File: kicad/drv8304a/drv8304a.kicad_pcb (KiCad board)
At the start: 2 copper layers, 37 parts, among them J1 Conn_01x05_Pin, J2 Conn_01x03_Pin, J3 Conn_01x05_Pin, Q1 CSD18514Q5A, Q2 CSD18514Q5A, Q3 CSD18514Q5A, Q4 CSD18514Q5A, Q5 CSD18514Q5A, Q6 CSD18514Q5A, U1 DRV8304H

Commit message: some routing
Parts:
- added C11: 1uF, Capacitor_SMD:C_0805_2012Metric_Pad1.18x1.45mm_HandSolder, F.Cu at (184.0, 84.5)
- added C12: 1uF, Capacitor_SMD:C_0805_2012Metric_Pad1.18x1.45mm_HandSolder, F.Cu at (184.0, 96.5)
- added C13: 1uF, Capacitor_SMD:C_0805_2012Metric_Pad1.18x1.45mm_HandSolder, F.Cu at (178.0, 108.5)
- added J4: Conn_01x02_Pin, Connector_PinHeader_2.54mm:PinHeader_1x02_P2.54mm_Vertical, F.Cu at (30.8, 26.8)
- moved Q1 159.9 mm to (190.0, 110.0), turned to 180 degrees
- moved Q2 155.0 mm to (190.0, 104.0)
- moved J2 151.9 mm to (200.0, 100.0), turned to 90 degrees
- moved Q3 150.9 mm to (190.0, 98.0), turned to 180 degrees
- moved Q4 147.9 mm to (190.0, 92.0)
- moved Q5 145.9 mm to (190.0, 86.0), turned to 180 degrees
- moved Q6 145.0 mm to (190.0, 80.0)
- moved R14 133.6 mm to (184.1, 105.5), turned to -90 degrees
- moved R15 125.3 mm to (173.0, 112.8)
- moved R16 125.3 mm to (173.0, 117.7)
- moved U1 118.8 mm to (170.0, 95.0), turned to 90 degrees
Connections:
- net Net-(J2-Pin_1) renamed /SHA
- net Net-(J2-Pin_2) renamed /SHB
- net Net-(J2-Pin_3) renamed /SHC
- net Net-(Q1-D) renamed VM
- net Net-(Q1-G) renamed /GHA
- net Net-(Q2-G) renamed /GLA
- net Net-(Q3-G) renamed /GHB
- net Net-(Q4-G) renamed /GLB
- net Net-(Q5-G) renamed /GHC
- net Net-(Q6-G) renamed /GLC
- net Net-(U1-SPA) renamed /SPA
- net Net-(U1-SPB) renamed /SPB
- net Net-(U1-SPC) renamed /SPC
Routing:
- net /GHA: track 0.00 -> 28.6 mm
- net /SHA: track 0.00 -> 26.6 mm
- net VM: track 0.00 -> 26.0 mm
- net /GLA: track 0.00 -> 21.0 mm

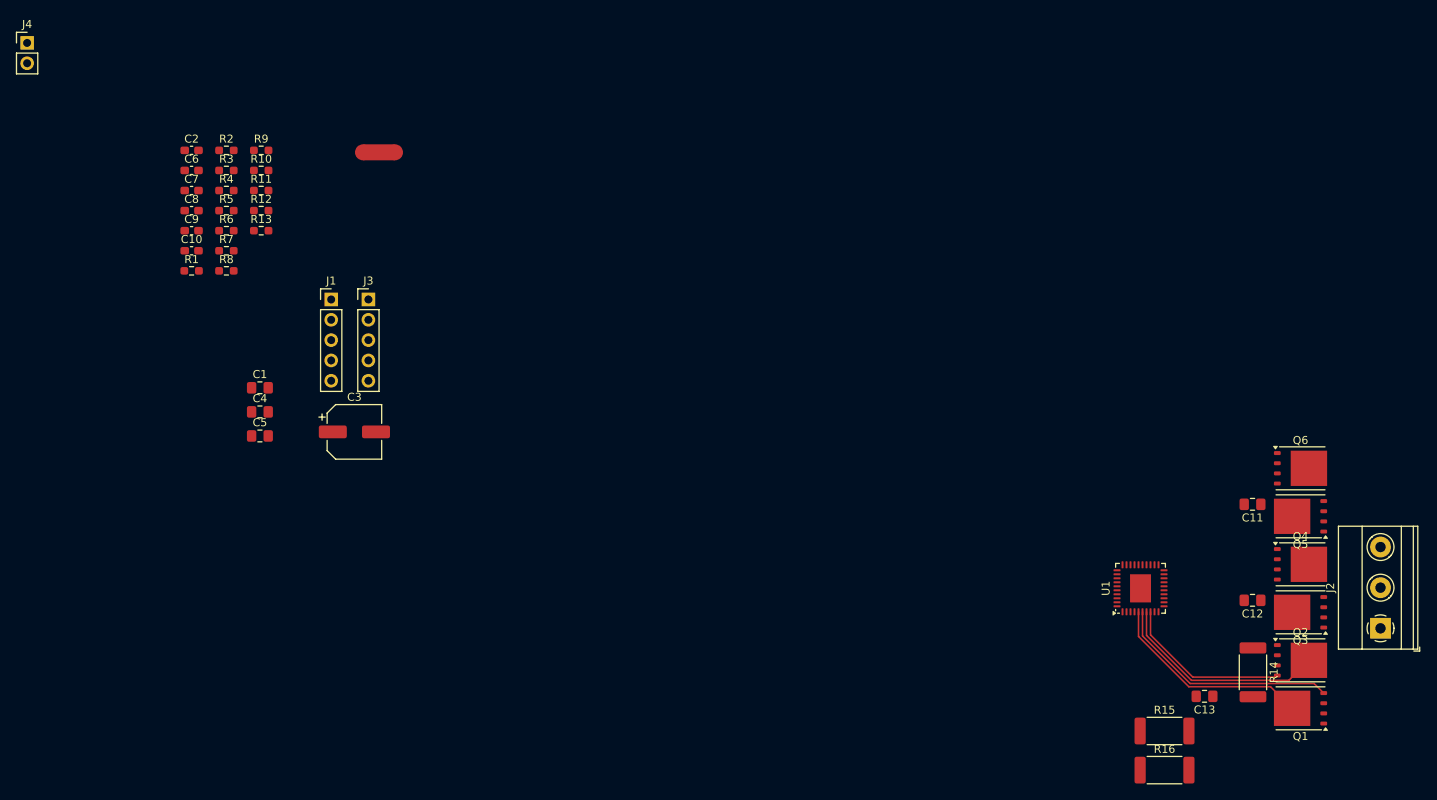
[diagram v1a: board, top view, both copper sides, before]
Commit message: FETS routed
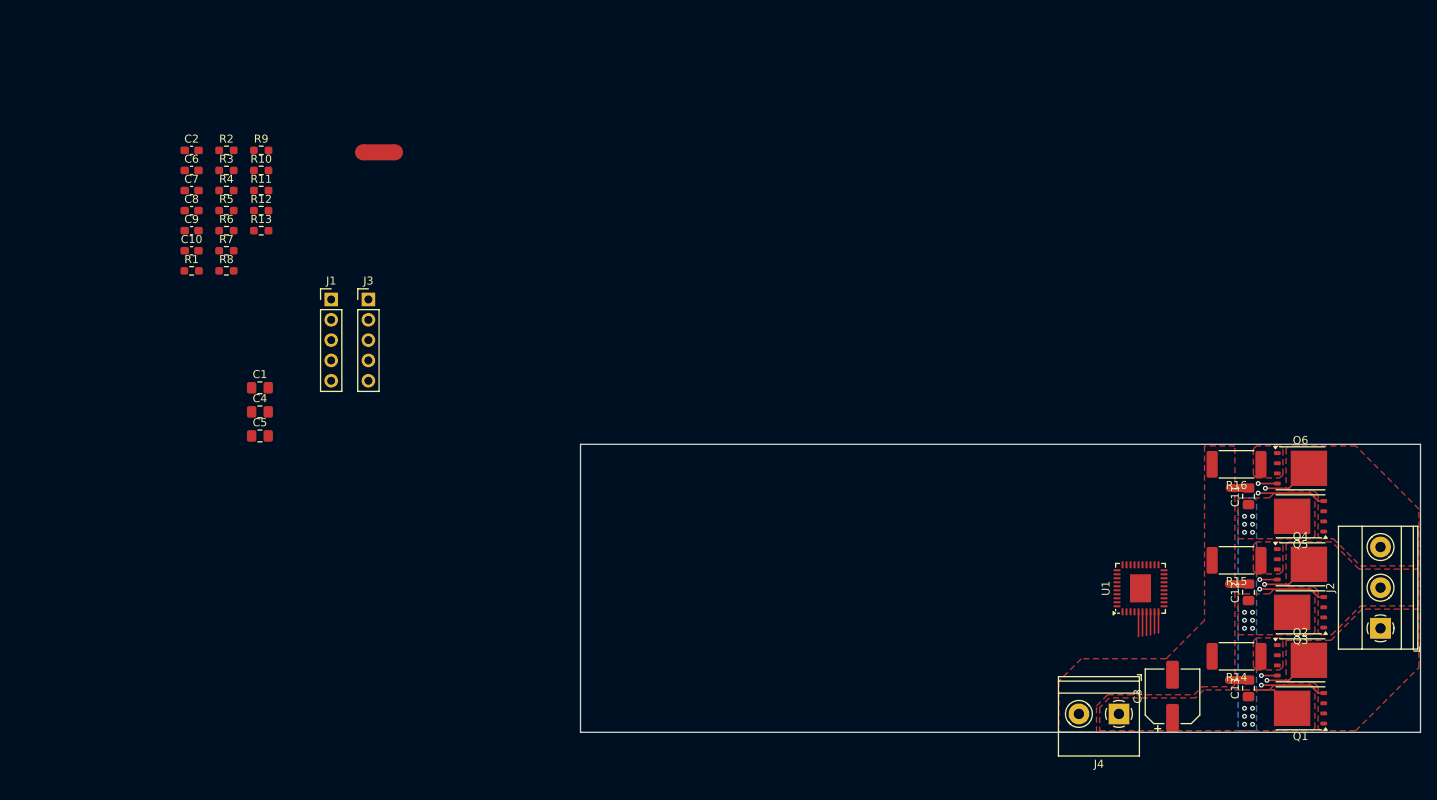
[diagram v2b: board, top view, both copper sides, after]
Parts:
- J4: footprint Connector_PinHeader_2.54mm:PinHeader_1x02_P2.54mm_Vertical -> TerminalBlock_Phoenix:TerminalBlock_Phoenix_MKDS-1,5-2_1x02_P5.00mm_Horizontal
- moved J4 160.2 mm to (167.3, 110.7), turned to 180 degrees
- moved C3 107.5 mm to (174.0, 108.5), turned to 90 degrees
- moved R16 39.3 mm to (182.0, 79.5), turned to 180 degrees
- moved R15 23.2 mm to (182.0, 91.5), turned to 180 degrees
- moved C13 5.59 mm to (183.5, 107.5), turned to 90 degrees
- moved R14 2.87 mm to (182.0, 103.5), turned to 180 degrees
- moved C11 1.12 mm to (183.5, 83.5), turned to 90 degrees
- moved C12 1.12 mm to (183.5, 95.5), turned to 90 degrees
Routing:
- net /GHA: track 28.6 -> 11.2 mm, vias 0 -> 1
- net /SHA: track 26.6 -> 9.24 mm, vias 0 -> 1
- net VM: track 26.0 -> 8.77 mm, vias 0 -> 18
- net /GLA: track 21.0 -> 4.88 mm, vias 0 -> 1
- net GNDPWR: track 0.00 -> 9.93 mm
- net /GHC: track 0.00 -> 8.68 mm, vias 0 -> 1
- net /GHB: track 0.00 -> 8.42 mm, vias 0 -> 1
- net /SHB: track 0.00 -> 6.59 mm, vias 0 -> 1
- net /SHC: track 0.00 -> 6.49 mm, vias 0 -> 1
- net /SPA: track 0.00 -> 3.66 mm
- net /GLC: track 0.00 -> 2.41 mm, vias 0 -> 1
- net /GLB: track 0.00 -> 2.20 mm, vias 0 -> 1
- added copper zone on F.Cu, net /SHA
- added copper zone on F.Cu, net /SHB
- added copper zone on F.Cu, net /SHC
- added copper zone on F.Cu, net /SPA
- added copper zone on F.Cu, net /SPB
- added copper zone on F.Cu, net /SPC
- added copper zone on F.Cu, net GNDPWR
- added copper zone on B.Cu, net VM
- added copper zone on F.Cu, net VM
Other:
- board outline added: 105 x 36 mm
- copper layers 2 -> 4

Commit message: lots routed
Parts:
- moved C2 132.9 mm to (169.6, 100.9)
- moved C6 122.6 mm to (161.7, 96.3), turned to 90 degrees
- moved C7 122.0 mm to (164.6, 90.8), turned to 180 degrees
- moved R2 121.4 mm to (169.9, 81.6), turned to 180 degrees
- moved R3 121.1 mm to (169.9, 83.1), turned to 180 degrees
- moved R1 121.1 mm to (169.9, 80.1), turned to 180 degrees
- moved R4 120.7 mm to (169.9, 84.6), turned to 180 degrees
- moved R5 120.4 mm to (169.9, 86.1), turned to 180 degrees
- moved C8 117.7 mm to (160.3, 92.5)
- moved C1 116.7 mm to (172.3, 101.5), turned to 90 degrees
- moved C9 115.8 mm to (160.3, 89.5)
- moved R9 114.9 mm to (166.1, 84.6), turned to 180 degrees
- moved R10 114.5 mm to (166.1, 86.1), turned to 180 degrees
- moved R6 114.3 mm to (166.1, 80.1), turned to 180 degrees
- moved R7 114.1 mm to (166.1, 81.6), turned to 180 degrees
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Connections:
- C7 pad 1: Net-(U1-VREF) -> VDD
- U1 pad 24: Net-(U1-VREF) -> VDD
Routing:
- net GNDPWR: track 9.93 -> 49.3 mm, vias 0 -> 3
- net VDD: track 0.00 -> 36.0 mm, vias 0 -> 3
- net GNDA: track 0.00 -> 24.9 mm, vias 0 -> 5
- net /SPC: track 0.00 -> 22.4 mm, vias 0 -> 2
- net VM: track 8.77 -> 30.5 mm, vias 18 -> 37
- net Net-(U1-VDS): track 0.00 -> 21.4 mm, vias 0 -> 2
- net /INL: track 0.00 -> 19.4 mm, vias 0 -> 3
- net Net-(U1-GAIN): track 0.00 -> 19.0 mm, vias 0 -> 2
- net Net-(U1-MODE): track 0.00 -> 18.8 mm, vias 0 -> 2
- net /INHA: track 0.00 -> 18.5 mm, vias 0 -> 1
- net /SHC: track 6.49 -> 24.8 mm, vias 1 -> 2
- net /GLC: track 2.41 -> 20.5 mm, vias 1 -> 2
- net Net-(U1-IDRIVE): track 0.00 -> 17.6 mm, vias 0 -> 2
- net /GHC: track 8.68 -> 25.8 mm, vias 1 -> 2
- net /INHB: track 0.00 -> 16.9 mm, vias 0 -> 1
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- added copper zone on In1.Cu, net GNDA
- added copper zone on In1.Cu, net VM
- removed copper zone on B.Cu, net VM
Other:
- board size 105 x 36 mm -> 50 x 36 mm

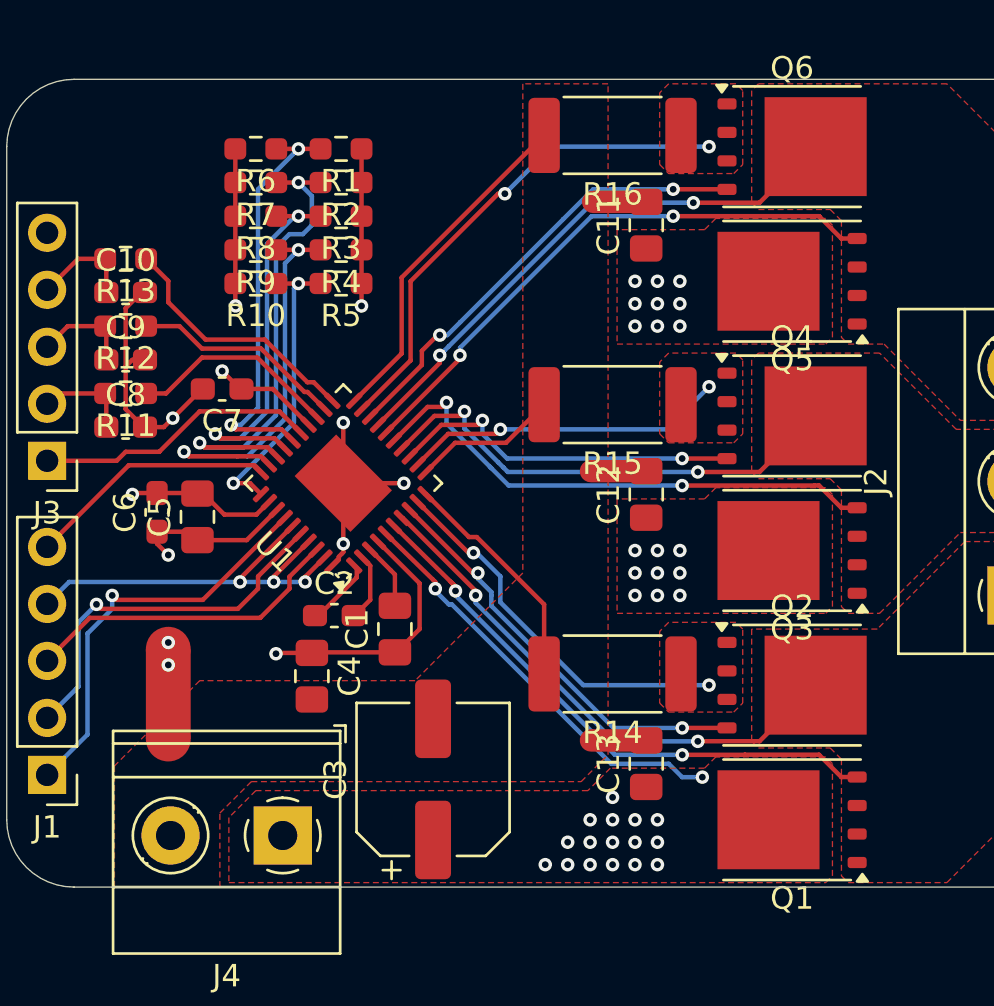
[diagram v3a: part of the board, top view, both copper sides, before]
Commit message: 100 % routed, supply layer thickend
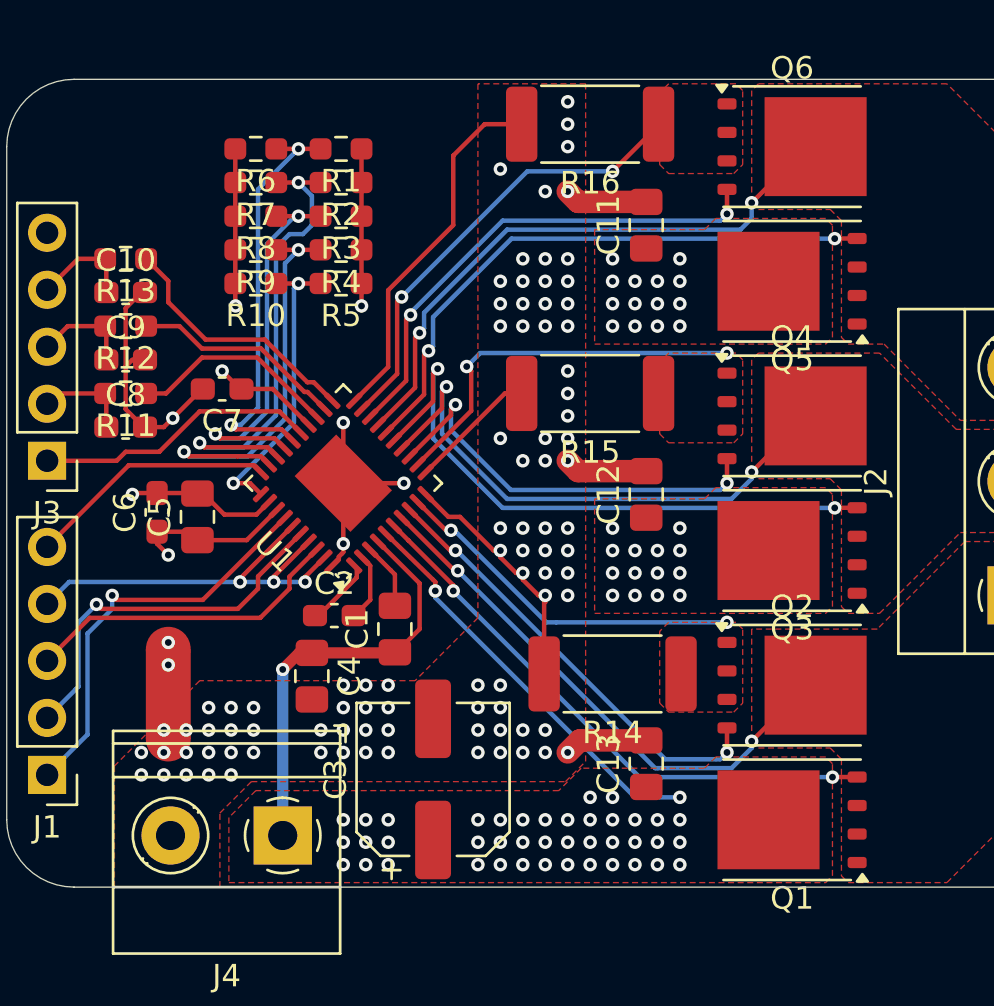
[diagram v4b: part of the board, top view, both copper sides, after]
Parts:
- moved R15 1.12 mm to (181.0, 91.0)
- moved R16 1.12 mm to (181.0, 79.0)
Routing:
- net VM: track 30.5 -> 37.4 mm, vias 37 -> 72
- net GNDPWR: track 49.3 -> 54.1 mm, vias 3 -> 92
- net /SHB: track 21.7 -> 25.3 mm
- net /GHB: track 24.2 -> 27.4 mm
- net /GLB: track 16.1 -> 19.0 mm
- net /SPB: track 14.4 -> 17.3 mm
- net /SPC: track 22.4 -> 20.4 mm
- net /SHC: track 24.8 -> 26.8 mm
- net /GLC: track 20.5 -> 22.4 mm
- net /GLA: track 18.7 -> 20.0 mm
- net /SPA: track 18.0 -> 17.0 mm
- net /SHA: track 23.9 -> 24.8 mm
- net /GHC: track 25.8 -> 26.4 mm
- added copper zone on In1.Cu, net GNDPWR

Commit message: DRV8304a done
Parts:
- R1, R10, R2, R3, R4, R5, R6, R7, R8, R9: value NC -> DNP
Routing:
- added copper zone on In2.Cu, net GNDPWR
- added copper zone on In2.Cu, net VM
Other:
- board text added: "2024-08-30 MEgli"
- board text added: "CAL"
- board text added: "DRV8304a driver board"
- board text added: "ENABLE"
- board text added: "GAIN"
- board text added: "GND"
- board text added: "GND VM"
- board text added: "GNDA"
- board text added: "IDRIVE"
- board text added: "INHA"
- board text added: "INHB"
- board text added: "INHC"
- board text added: "INL"
- board text added: "MODE"
- board text added: "SOA"
- board text added: "SOB"
- board text added: "SOC"
- board text added: "VDC"
- board text added: "VDD"
- board text added: "nFAULT"
